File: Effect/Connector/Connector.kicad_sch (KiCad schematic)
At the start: 20 parts, among them J1 Conn_01x04_Pin, J2 Conn_01x05_Pin, J4 RJ45_LED_Shielded, J5 USB_C_Receptacle_USB2.0_16P, U1 TLE2426xD, U2 OPA1656

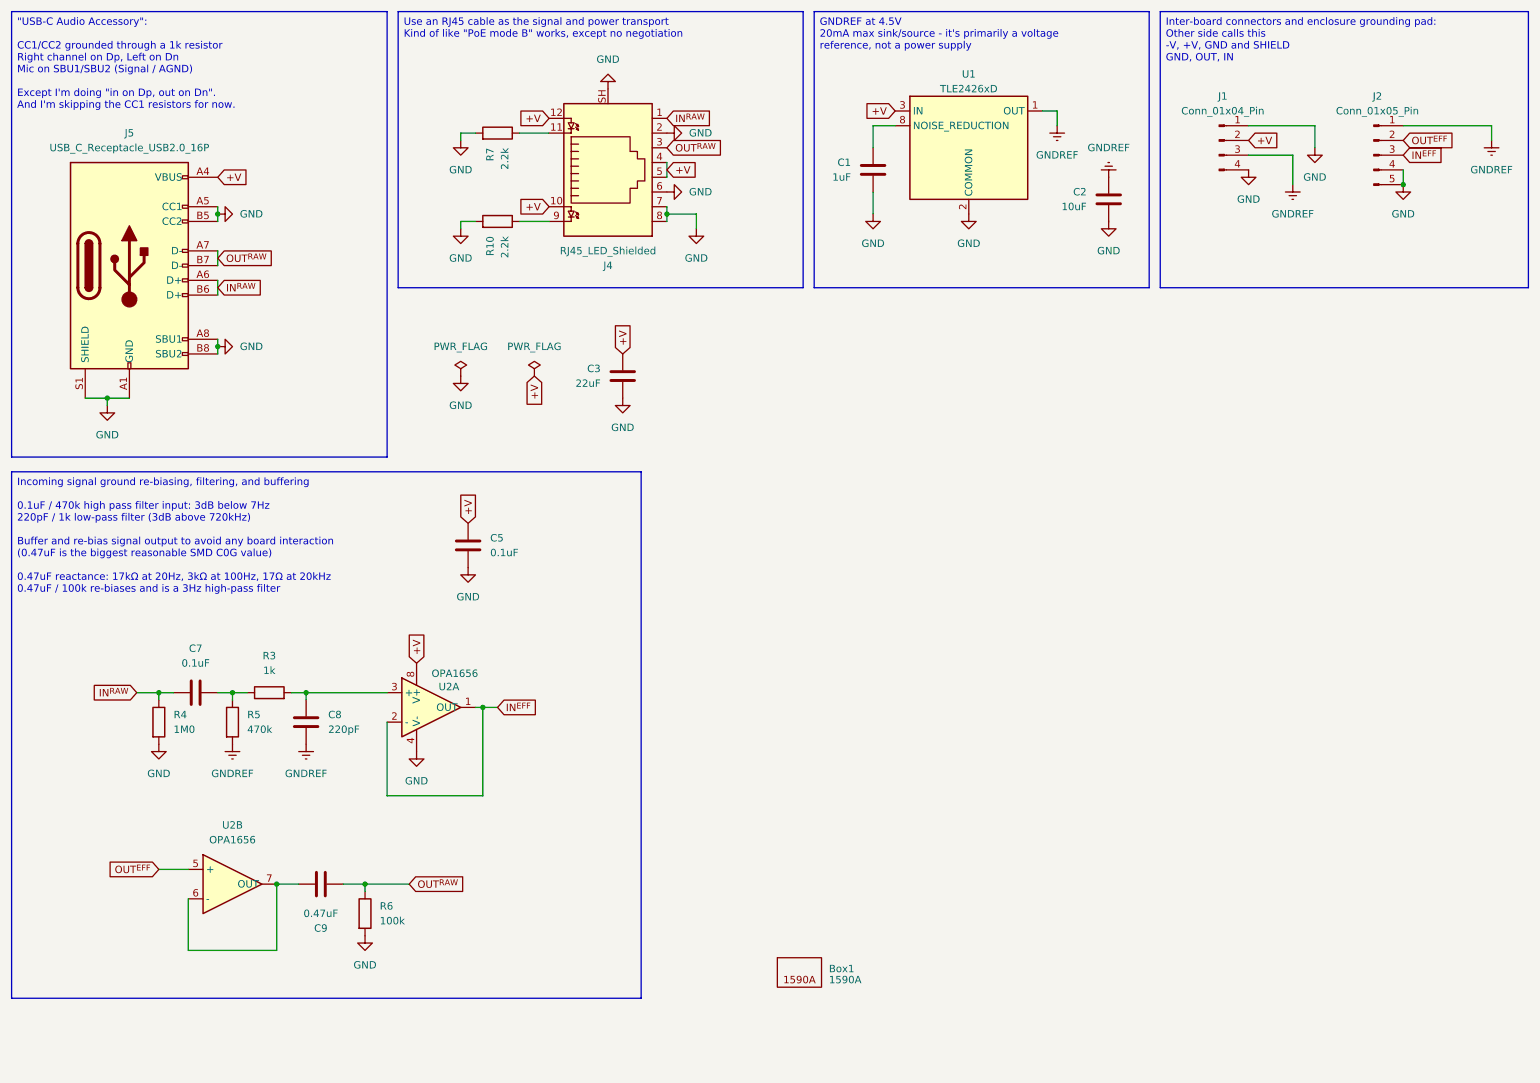
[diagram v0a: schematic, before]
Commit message: Simplify the connector testing to just a USB-C connector
This is mainly to see what that would look like, particularly for the
base that now becomes really simple and small.

The effect connector ends up being crazy large just because of the old
pin header layout.  But the point of all this is that if it works out,
we'll dispense with the pin headers, and just use the USB-C connector
"natively".

So the effects board is just a temporary thing, and the base board is
where it's at.  If the base board works well, and I can stop soldering
stomp switches, I'll be good.

Signed-off-by: Linus Torvalds <torvalds@linux-foundation.org>
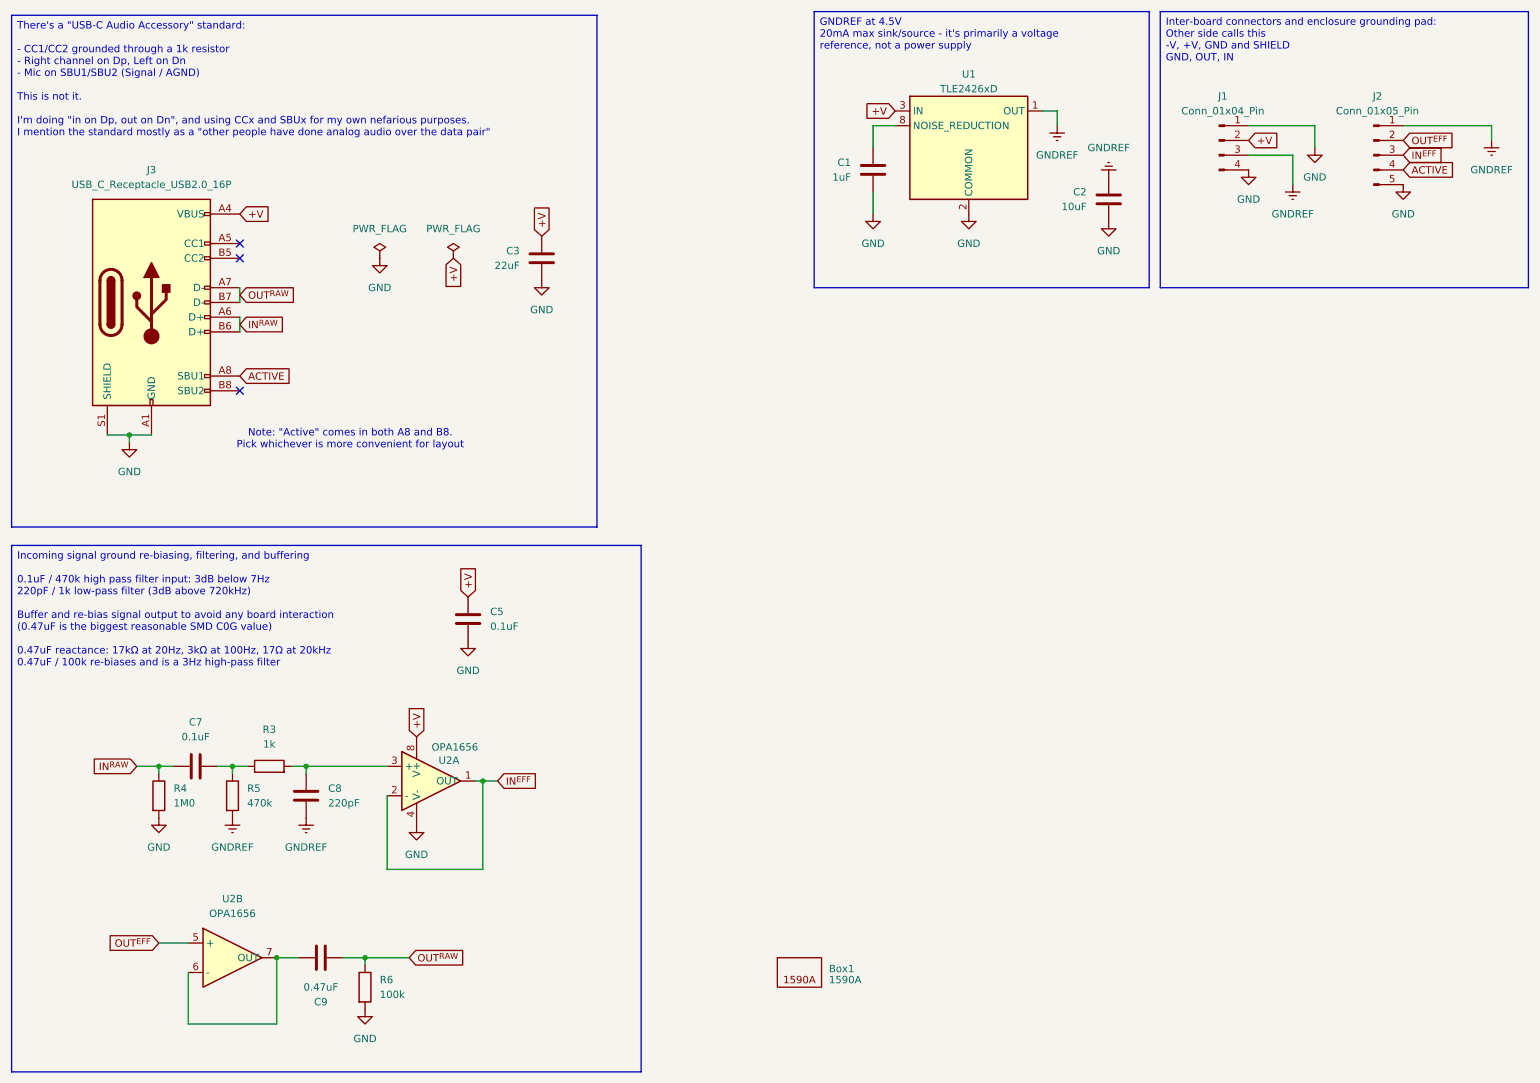
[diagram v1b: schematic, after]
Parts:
- removed J4: RJ45_LED_Shielded, Connector_RJ:RJ45_Amphenol_RJHSE538X, symbol Connector:RJ45_LED_Shielded
- removed J5: USB_C_Receptacle_USB2.0_16P, Connector_USB:USB_C_Receptacle_GCT_USB4085, symbol Connector:USB_C_Receptacle_USB2.0_16P
- removed R10, R7: 2.2k, Resistor_SMD:R_0805_2012Metric_Pad1.20x1.40mm_HandSolder, symbol Device:R
- added J3: USB_C_Receptacle_USB2.0_16P, Connector_USB:USB_C_Receptacle_GCT_USB4085, symbol Connector:USB_C_Receptacle_USB2.0_16P
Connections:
- net +V: now also J3.A4 (VBUS), J3.A9 (VBUS), J3.B4 (VBUS), J3.B9 (VBUS)
- net GND: now also J3.A1 (GND), J3.A12 (GND), J3.B1 (GND), J3.B12 (GND), J3.S1 (SHIELD); no longer J2.4 (Pin_4)
- net IN^{RAW}: now also J3.A6 (D+), J3.B6 (D+)
- net OUT^{RAW}: now also J3.A7 (D-), J3.B7 (D-)
- new net ACTIVE: J2.4 (Pin_4), J3.A8 (SBU1)
- no-connect marks 0 -> 3
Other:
- note added: "Note: "Active" comes in both A8 and B8. Pick whichever is more convenient for layout"
- moved on the sheet: C3, C5, C7, C8, C9, R3, R4, R5, R6, U2A, U2B
